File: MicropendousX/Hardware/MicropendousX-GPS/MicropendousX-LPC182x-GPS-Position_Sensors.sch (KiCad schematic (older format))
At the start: 12 parts, among them IC1 LPC182x, U2 PA6C_GPS_MODULE

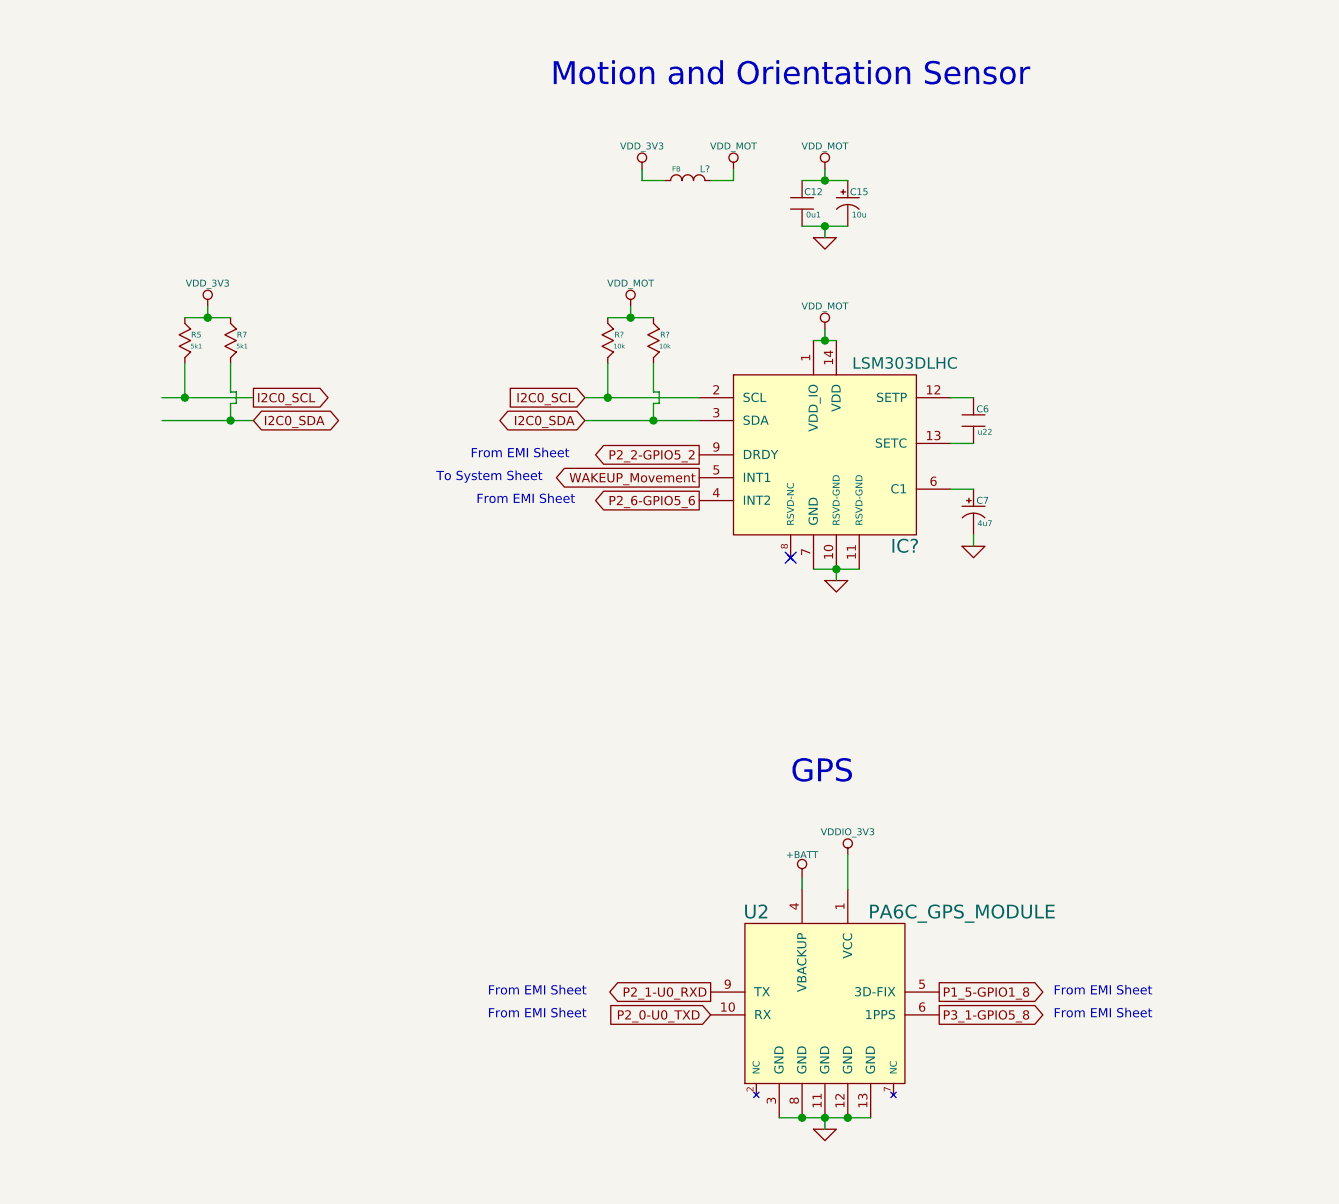
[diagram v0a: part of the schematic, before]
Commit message: Updated MicropendousX-LPC182x-GPS design.  PCB routing almost complete.
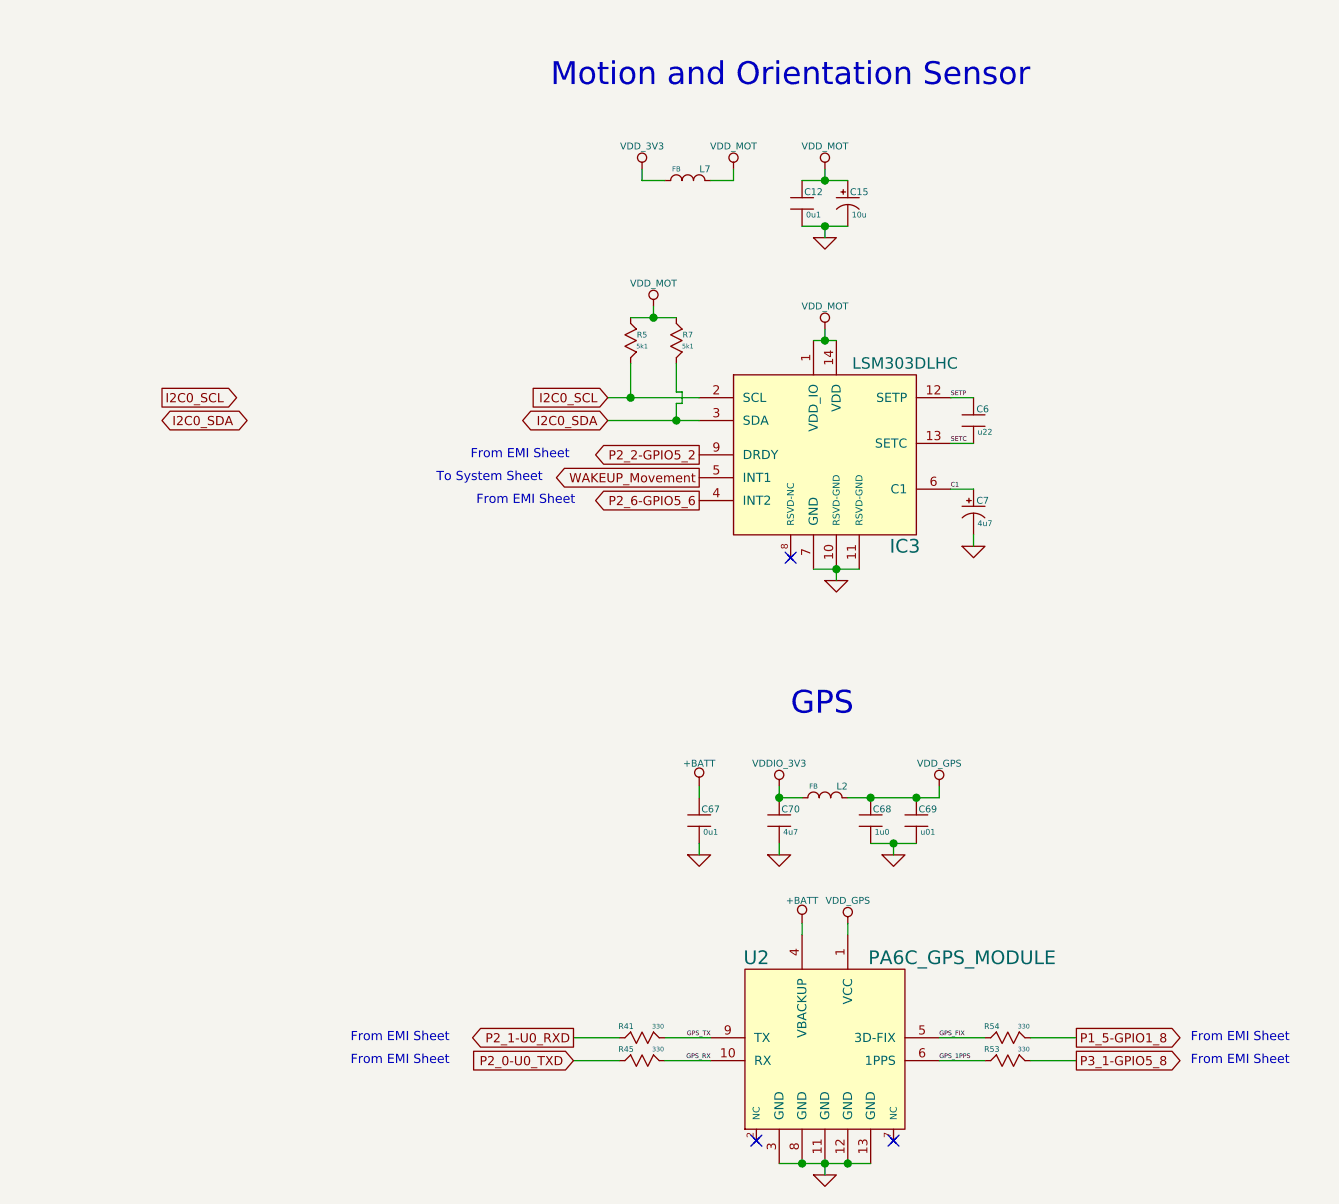
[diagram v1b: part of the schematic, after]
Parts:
- removed R? (x2): 10k, symbol R_MINI
- added C67: 0u1, symbol C_MINI
- added C68: 1u0, symbol C_MINI
- added C69: u01, symbol C_MINI
- added C70: 4u7, symbol C_MINI
- added L2: FB, symbol L_MINI
- added R41, R45, R53, R54: 330, symbol R_MINI
- gave numbers to parts that had none: 2
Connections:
- net labels added: C1, GPS_1PPS, GPS_FIX, GPS_RX, GPS_TX, SETC, SETP, VDD_GPS
- wire segments 40 -> 47
- no-connect marks 1 -> 3
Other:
- moved on the sheet: R5, R7, U2

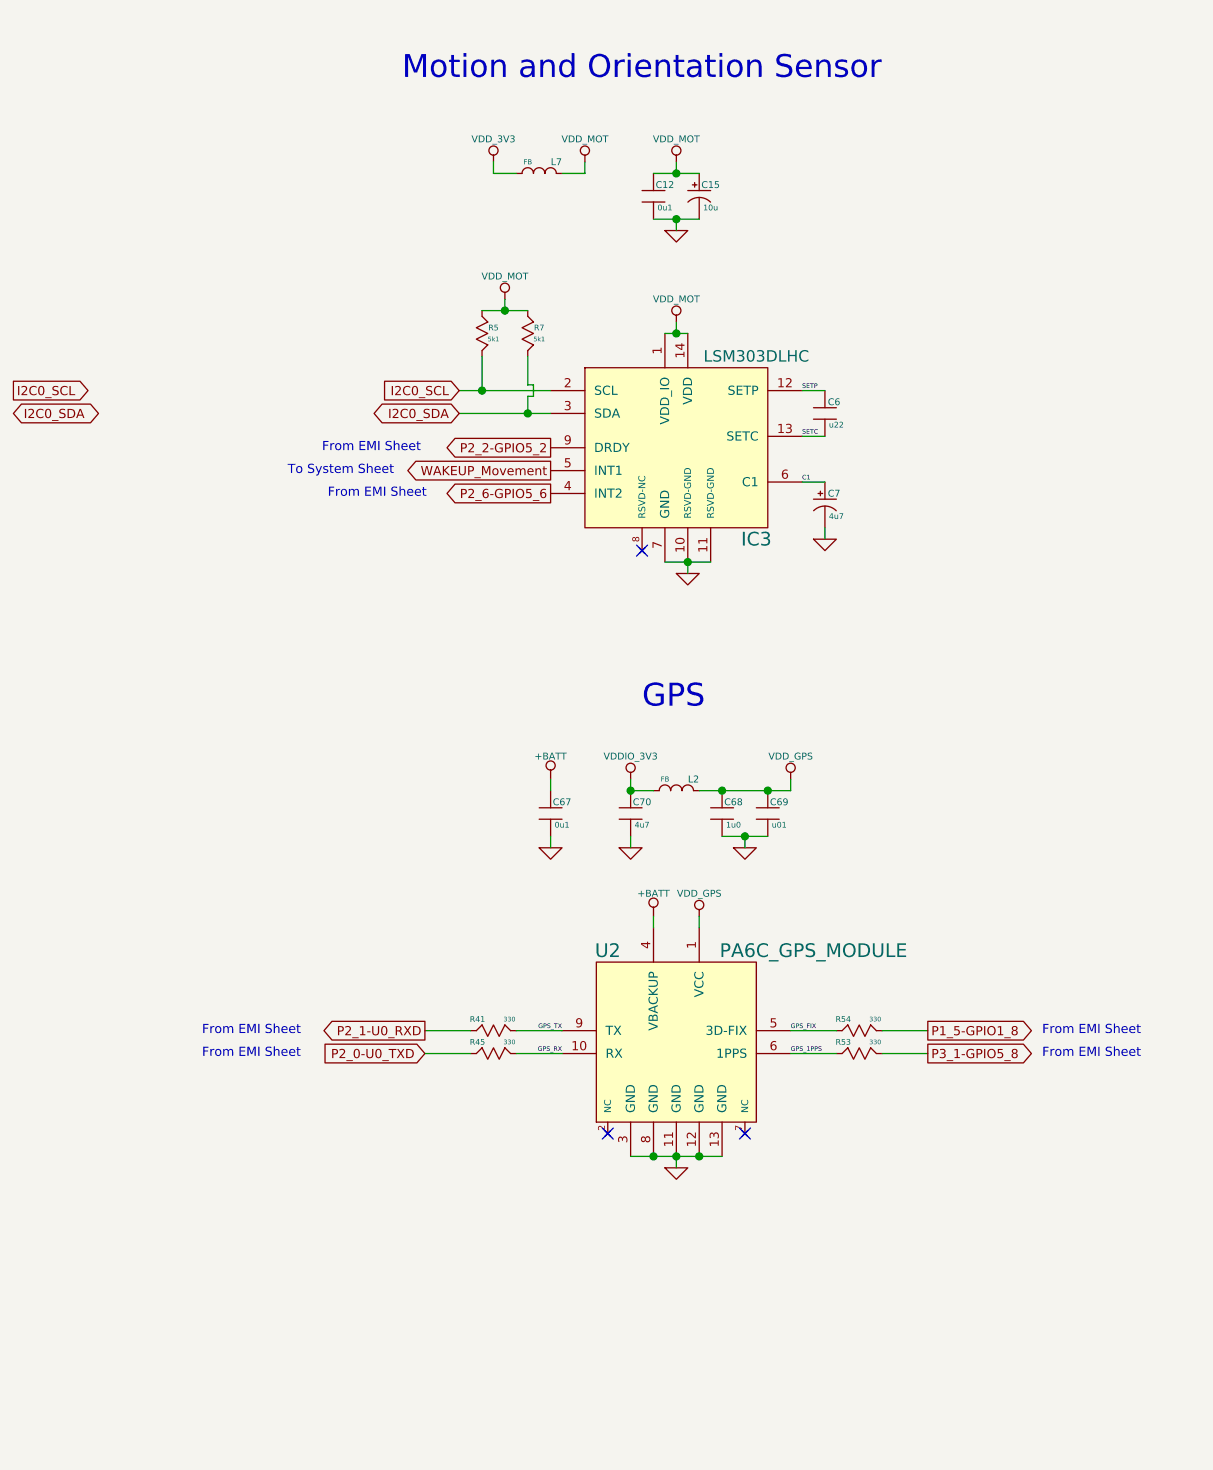
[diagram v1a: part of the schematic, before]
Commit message: Updated MicropendousX-LPC182x-GPS design. PCB routing is complete.
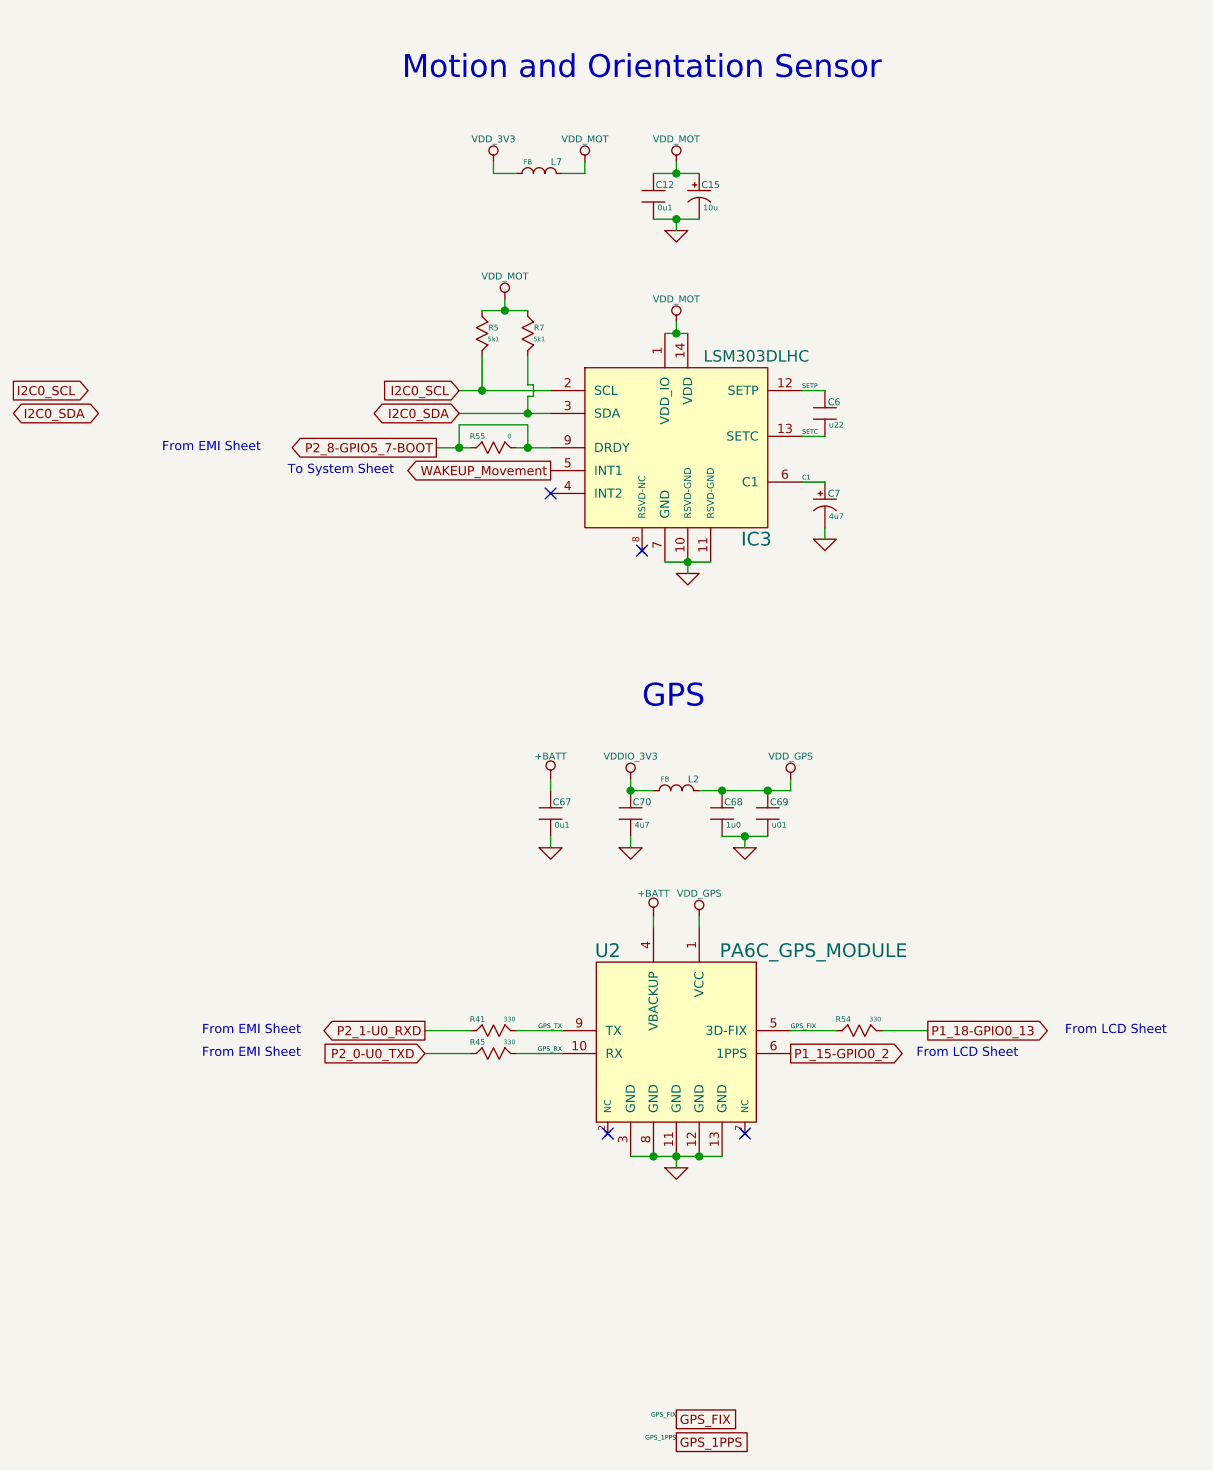
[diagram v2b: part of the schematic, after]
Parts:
- removed R53: 330, symbol R_MINI
- added R55: 0, symbol R_MINI
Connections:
- net labels added: P1_15-GPIO0_2, P1_18-GPIO0_13, P2_8-GPIO5_7-BOOT
- net labels removed: P1_5-GPIO1_8, P2_2-GPIO5_2, P2_6-GPIO5_6, P3_1-GPIO5_8
- wire segments 47 -> 50
- no-connect marks 3 -> 4
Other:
- note added: "From LCD Sheet"
